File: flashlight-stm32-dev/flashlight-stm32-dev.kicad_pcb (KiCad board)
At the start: 6 copper layers, 120 x 35 mm, 91 parts, among them J1 USB_C_Receptacle, J2 ST-LINK, J3 IO1, J4 IO2, Q1 2N7002H, Q2 2N7002H, Q3 2N7002H, SW1 RESET, SW2 BOOT, U1 BQ25185DLHR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

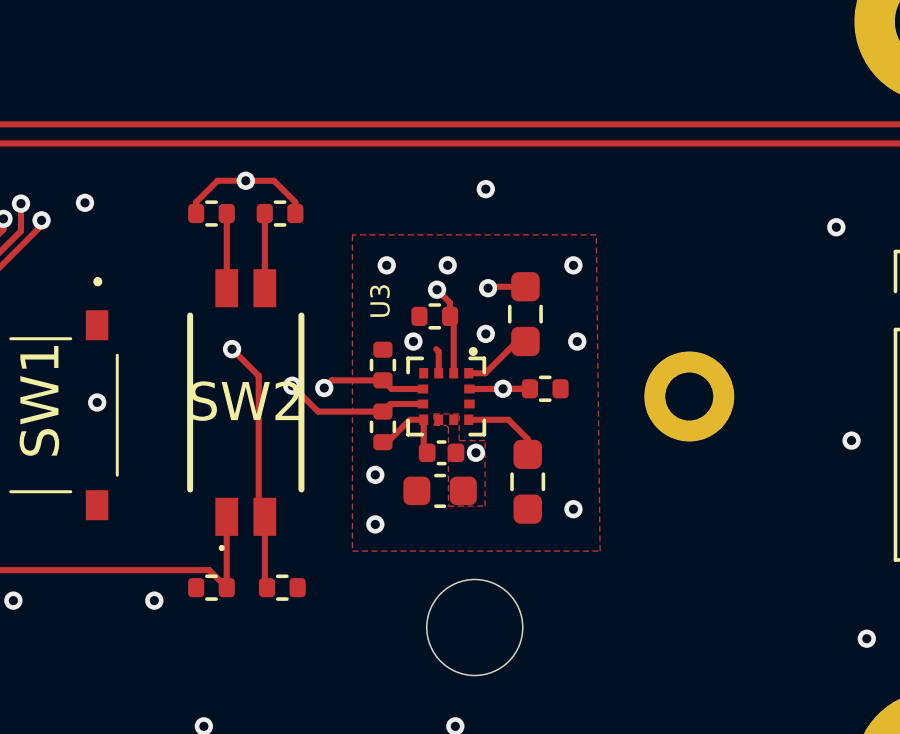
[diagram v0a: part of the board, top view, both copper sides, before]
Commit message: updated accel and usbc cc
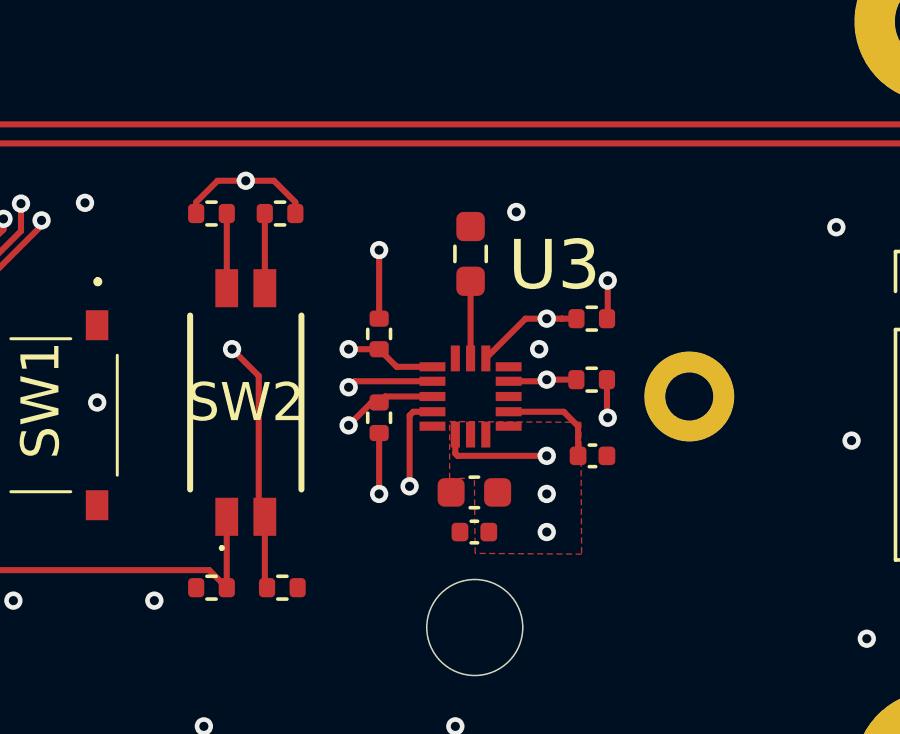
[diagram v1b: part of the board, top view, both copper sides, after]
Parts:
- removed the RU33 at (198.7, 126.6)
- added CU33: 100n, Capacitor_SMD:C_0402_1005Metric, F.Cu at (200.9, 131.3)
- U3: value BMA400 -> MMA8451QR1; footprint BMA400:XDCR_BMA400 -> MMA8451QR1:QFN50P300X300X100-16N
- moved RU33 7.83 mm to (196.8, 124.6)
- moved RU32 5.64 mm to (200.9, 128.8), turned to 0 degrees
- moved RU35 3.10 mm to (193.8, 127.3), turned to 90 degrees
- moved CU32 2.86 mm to (197.0, 133.9), turned to 180 degrees
- moved RU31 2.80 mm to (200.9, 126.7)
- moved RU36 1.76 mm to (193.8, 130.0), turned to 90 degrees
- moved CU31 1.14 mm to (197.0, 132.5), turned to 180 degrees
- moved U3 0.81 mm to (196.8, 129.3), turned to 180 degrees
- renumbered RU34 to RU33
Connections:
- RU31 pad 1: /SCL -> /SDA
- RU32 pad 1: /SDA -> /SCL
- RU33 pad 1: Net-(U3-~{CSB}) -> GND
- RU33 pad 2: +3.3V -> Net-(U3-SA0)
- U3 pad 1: Net-(U3-SDO) -> +3.3V
- U3 pad 10: Net-(U3-~{CSB}) -> GND
- U3 pad 11: unconnected-(U3-NC-Pad11) -> /INT1
- U3 pad 12: /SCL -> GND
- U3 pad 2: /SDA -> Net-(U3-BYP)
- U3 pad 3: +3.3V -> unconnected-(U3-NC_2-Pad3)
- U3 pad 4: unconnected-(U3-NC-Pad4) -> /SCL
- U3 pad 5: /INT1 -> GND
- U3 pad 6: /INT2 -> /SDA
- U3 pad 7: +3.3V -> Net-(U3-SA0)
- U3 pad 8: GND -> unconnected-(U3-NC_5-Pad8)
- U3 pad 9: GND -> /INT2
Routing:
- net +3.3V: track 43.2 -> 50.2 mm, vias 26 -> 24
- net GND: track 14.3 -> 19.0 mm, vias 84 -> 85
- net /SDA: track 43.3 -> 47.9 mm
- net Net-(U3-BYP): track 0.00 -> 3.50 mm
- net Net-(U3-~{CSB}): track 2.74 -> 0.00 mm
- net Net-(U3-SA0): track 0.00 -> 2.57 mm
- net Net-(U3-SDO): track 2.33 -> 0.00 mm
- net /SCL: track 41.4 -> 42.1 mm

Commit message: final for review
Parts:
- added TP1: STAT1_TP, TestPoint:TestPoint_Pad_D2.0mm, F.Cu at (124.3, 84.3)
- added TP2: STAT2_TP, TestPoint:TestPoint_Pad_D2.0mm, F.Cu at (126.7, 81.3)
- added TP3: CE_TP, TestPoint:TestPoint_Pad_D2.0mm, F.Cu at (160.7, 84.3)
- added TP4: 5V_TP, TestPoint:TestPoint_Pad_D2.0mm, F.Cu at (99.1, 105.3)
- added TP5: 33V_TP, TestPoint:TestPoint_Pad_D2.0mm, F.Cu at (116.3, 81.2)
- added TP6: VS_TP, TestPoint:TestPoint_Pad_D2.0mm, F.Cu at (103.6, 102.5)
- added TP7: SCL_TP, TestPoint:TestPoint_Pad_D2.0mm, F.Cu at (195.1, 98.2)
- added TP8: SDA_TP, TestPoint:TestPoint_Pad_D2.0mm, F.Cu at (193.0, 86.5)
- RJ11, RJ12: value 22k -> 5.1k
- moved RJ11 39.7 mm to (98.1, 96.8), turned to -90 degrees
- moved JP1 38.5 mm to (148.3, 101.3)
- moved D1 38.4 mm to (99.3, 82.0)
- moved D4 38.0 mm to (91.3, 84.6)
- moved RD41 38.0 mm to (94.1, 84.6)
- moved CU14 37.8 mm to (112.2, 92.7)
- moved CU32 37.8 mm to (187.3, 97.3)
- moved RD13 37.8 mm to (123.3, 96.1)
- moved RU13 37.8 mm to (117.2, 89.2)
- moved U5 37.8 mm to (110.0, 102.9)
- moved BT1 37.8 mm to (156.4, 92.8)
- moved CU13 37.8 mm to (109.0, 93.1)
- moved CU16 37.8 mm to (110.9, 96.4)
- moved CU22 37.8 mm to (151.0, 86.6)
- moved CU31 37.8 mm to (187.4, 96.0)
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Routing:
- net /STAT2: track 53.1 -> 67.7 mm, vias 2 -> 3
- net +5V: track 13.6 -> 26.0 mm, vias 7 -> 8
- net /STAT1: track 56.1 -> 66.9 mm, vias 3 -> 4
- net /CE: track 68.5 -> 78.9 mm, vias 0 -> 2
- net /SCL: track 42.1 -> 51.1 mm, vias 2 -> 3
- net +3.3V: track 50.2 -> 43.6 mm
- net /SDA: track 47.9 -> 53.0 mm
- net Net-(J1-CC1): track 6.09 -> 3.33 mm
- net Net-(J1-CC2): track 9.65 -> 7.24 mm, vias 0 -> 2
- net GND: track 19.0 -> 18.3 mm, vias 85 -> 86
- net Net-(D1-GK): track 28.5 -> 29.2 mm
- net VS: vias 21 -> 20
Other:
- board text added: "+5V"
- board text added: "3.3"
- board text added: "3.3V"
- board text added: "32kHz"
- board text added: "5V"
- board text added: "8mhz"
- board text added: "A1"
- board text added: "A10"
- board text added: "A15"
- board text added: "A2"
- board text added: "A3"
- board text added: "A4"
- board text added: "A5"
- board text added: "A6"
- board text added: "A7"
- board text added: "A8"
- board text added: "A9"
- board text added: "B10"
- board text added: "B11"
- board text added: "B12"
- board text added: "B13"
- board text added: "B14"
- board text added: "B15"
- board text added: "B3"
- board text added: "BAT+"
- board text added: "BAT-"
- board text added: "BOOT0"
- board text added: "BOOT1"
- board text added: "BVRG"
- board text added: "By Ahmad Taka takaahmad25@gmail.com Rev 1.1"
- board text added: "CE"
- board text added: "GD"
- board text added: "GND"
- board text added: "RESET"
- board text added: "SCL"
- board text added: "SD"
- board text added: "SDA"
- board text added: "SK"
- board text added: "STAT1"
- board text added: "STAT2"
- board text added: "STM32L151C8 BATTERY DEV BOARD"
- board text added: "SWD"
- board text added: "SYS"
- board text added: "VADC"
- board text added: "VS"
- board text added: "x"
- board text added: "y"
- board text added: "z"

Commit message: updates
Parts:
- removed RU22: 0, Resistor_SMD:R_0603_1608Metric_Pad0.98x0.95mm_HandSolder
- added CU210: 100n, Capacitor_SMD:C_0603_1608Metric_Pad1.08x0.95mm_HandSolder, F.Cu at (147.6, 87.6)
- D1: footprint LED_THT:LED_D5.0mm-4_RGB_Staggered_Pins -> 19-237_R6GHBHC-A01_2T:19237R6GHBHCA012T
- J3, J4: footprint Connector_PinHeader_2.54mm:PinHeader_1x11_P2.54mm_Vertical -> Connector_PinHeader_2.54mm:PinHeader_1x12_P2.54mm_Vertical
- moved J3 2.54 mm to (141.2, 108.4)
- moved J4 2.54 mm to (141.2, 77.5)
- moved D1 1.69 mm to (99.1, 80.4), turned to 180 degrees
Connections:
- D1 pad 1: Net-(D1-BK) -> Net-(D1-RK)
- D1 pad 2: +3.3V -> Net-(D1-GK)
- D1 pad 3: Net-(D1-RK) -> Net-(D1-BK)
- D1 pad 4: Net-(D1-GK) -> +3.3V
- J3 pad 1: /PA1 -> GND
- J3 pad 10: +3.3V -> /PB11
- J3 pad 11: GND -> +3.3V
- J3 pad 2: /PA2 -> /PA1
- J3 pad 3: /PA3 -> /PA2
- J3 pad 4: /PA4 -> /PA3
- J3 pad 5: /PA5 -> /PA4
- J3 pad 6: /PA6 -> /PA5
- J3 pad 7: /PA7 -> /PA6
- J3 pad 8: /PB10 -> /PA7
- J3 pad 9: /PB11 -> /PB10
- J4 pad 1: +3.3V -> /VLCD
- J4 pad 10: /PB13 -> /PB14
- J4 pad 11: /PB12 -> /PB13
- J4 pad 2: GND -> +3.3V
- J4 pad 3: /PB3 -> GND
- J4 pad 4: /PA15 -> /PB3
- J4 pad 5: /PA10 -> /PA15
- J4 pad 6: /PA9 -> /PA10
- J4 pad 7: /PA8 -> /PA9
- J4 pad 8: /PB15 -> /PA8
- J4 pad 9: /PB14 -> /PB15
- U2 pad 1: Net-(U2-VLCD) -> /VLCD
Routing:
- net /VLCD: track 0.00 -> 21.2 mm, vias 0 -> 1
- net Net-(U2-VLCD): track 4.84 -> 0.00 mm
- net Net-(D1-RK): track 32.2 -> 30.2 mm
- net Net-(D1-GK): track 29.2 -> 31.1 mm
- net Net-(D1-BK): track 32.7 -> 34.2 mm
- net +3.3V: track 43.6 -> 44.8 mm, vias 24 -> 25
- net GND: vias 86 -> 84
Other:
- board text added: "VLC"

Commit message: jlc result
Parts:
- removed RSW11: 100, Resistor_SMD:R_0402_1005Metric
- removed RSW12: 10k, Resistor_SMD:R_0402_1005Metric
- added J5: SYS, Connector_Pin:Pin_D1.3mm_L11.0mm, F.Cu at (202.8, 85.4)
- added J6: GND, Connector_Pin:Pin_D1.3mm_L11.0mm, F.Cu at (202.8, 100.5)
- CU16: value 1u -> 10u
- CU17: value 100n -> 1u
- D1: footprint 19-237_R6GHBHC-A01_2T:19237R6GHBHCA012T -> LED-SMD_4P-L1.6-W1.6-BR-RD:LED-SMD_4P-L1.6-W1.6-BR-RD
- RU31, RU32: value 10k -> 4.7k
- RU35, RU36: value 10k -> DNP; footprint Resistor_SMD:R_0402_1005Metric -> Resistor_SMD:R_0603_1608Metric_Pad0.98x0.95mm_HandSolder
- U3: value MMA8451QR1 -> MMA8452QR1; footprint MMA8451QR1:QFN50P300X300X100-16N -> MMA8452QR1:PQFN50P300X300X100-16N
- moved CSW11 1.15 mm to (168.0, 92.9)
- moved RU36 0.91 mm to (184.3, 94.4)
- moved RU35 0.43 mm to (184.3, 90.2)
- moved D1 0.40 mm to (99.4, 80.2)
- turned CU33 to 180 degrees
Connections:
- CU33 pad 1: Net-(U3-BYP) -> GND
- CU33 pad 2: GND -> Net-(U3-BYP)
- D1 pad 3: Net-(D1-BK) -> +3.3V
- D1 pad 4: +3.3V -> Net-(D1-BK)
- SW1 pad 2: Net-(RSW11-Pad1) -> /NRST
- U3 pad 13: unconnected-(U3-NC_3-Pad13) -> (no net)
- U3 pad 15: unconnected-(U3-NC_4-Pad15) -> (no net)
- U3 pad 16: unconnected-(U3-NC-Pad16) -> (no net)
- U3 pad 3: unconnected-(U3-NC_2-Pad3) -> (no net)
- U3 pad 8: unconnected-(U3-NC_5-Pad8) -> (no net)
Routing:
- net Net-(RSW11-Pad1): track 9.26 -> 0.00 mm
- net /NRST: track 17.7 -> 26.8 mm
- net /SWD: track 55.0 -> 48.1 mm
- net /SCK: track 59.2 -> 53.2 mm, vias 0 -> 1
- net Net-(D1-GK): track 31.1 -> 26.5 mm
- net /VLCD: track 21.2 -> 23.6 mm
- net +3.3V: track 44.8 -> 42.7 mm, vias 25 -> 27
- net Net-(D1-RK): track 30.2 -> 31.8 mm, vias 0 -> 2
- net Net-(D1-BK): track 34.2 -> 33.3 mm
- net GND: vias 84 -> 77
- net VS: vias 20 -> 46
- added copper zone on In4.Cu, net +3.3V
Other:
- board text added: "RGAB"
- board text removed: "BVRG"
